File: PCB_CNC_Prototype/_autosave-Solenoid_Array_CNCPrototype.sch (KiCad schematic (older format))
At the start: 10 parts, among them J1 Conn_01x02, J16 Power Daisy Chain_input, J3 Conn_01x01, Q1 AOD508

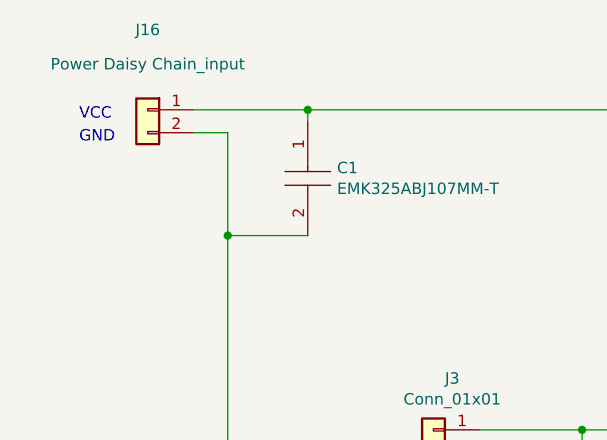
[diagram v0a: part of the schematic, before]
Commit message: revised connectors placement
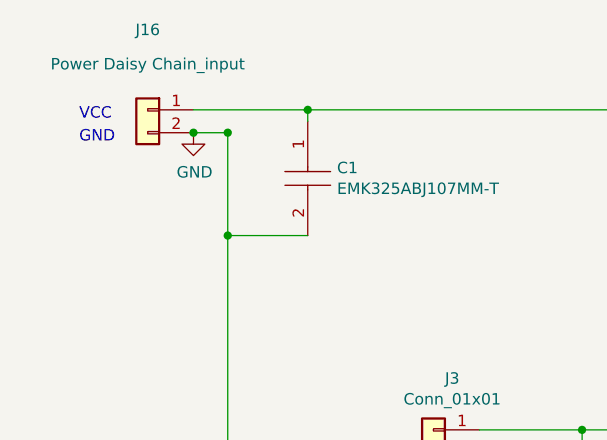
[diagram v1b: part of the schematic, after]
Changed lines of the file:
@@
 Wire Wire Line
 	1450 1050 1450 1500
+$Comp
+L power:GND #PWR0101
+U 1 1 5EC91A91
+P 1300 1050
+F 0 "#PWR0101" H 1300 800 50  0001 C CNN
+F 1 "GND" H 1305 877 50  0000 C CNN
+F 2 "" H 1300 1050 50  0001 C CNN
+F 3 "" H 1300 1050 50  0001 C CNN
+	1    1300 1050
+	1    0    0    -1
+$EndComp
+Connection ~ 1450 1050
+Connection ~ 1300 1050
 $EndSCHEMATC
